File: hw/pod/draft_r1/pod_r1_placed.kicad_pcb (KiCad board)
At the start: 4 copper layers, 34 x 13 mm, 76 parts, among them J1 TestPoint_Pad_D1.0mm, J10 TestPoint_Pad_D1.0mm, J11 TestPoint_Pad_D1.0mm, J12 TestPoint_Pad_D1.0mm, J2 TestPoint_Pad_D1.0mm, J3 TestPoint_Pad_D1.0mm, J4 TestPoint_Pad_D1.0mm, J5 TestPoint_Pad_D1.0mm, J6 TestPoint_Pad_D1.0mm, J7 TestPoint_Pad_D1.0mm, J8 TestPoint_Pad_D1.0mm, J9 TestPoint_Pad_D1.0mm, Q1 SOT1216_L1.1-W1.0-P0.35-BL-EP, Q2 SOT1216_L1.1-W1.0-P0.35-BL-EP, SW1 SW-SMD_4P-L3.0-W2.6-P1.85-LS3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, U1 QFN-48-1EP_7x7mm_P0.5mm_EP5.6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, U2 Knowles_LGA-5_3.5x2.65mm, U3 DSBGA-8_L1.6-W0.9-R2-C4-P0.40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, U4 X2SON-4_L1.0-W1.0-P0.65-TL-EP, U6 SOT-553-5_L1.6-W1.2-P0.50-LS1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, Y1 FC-135R_L3.2-W1.5

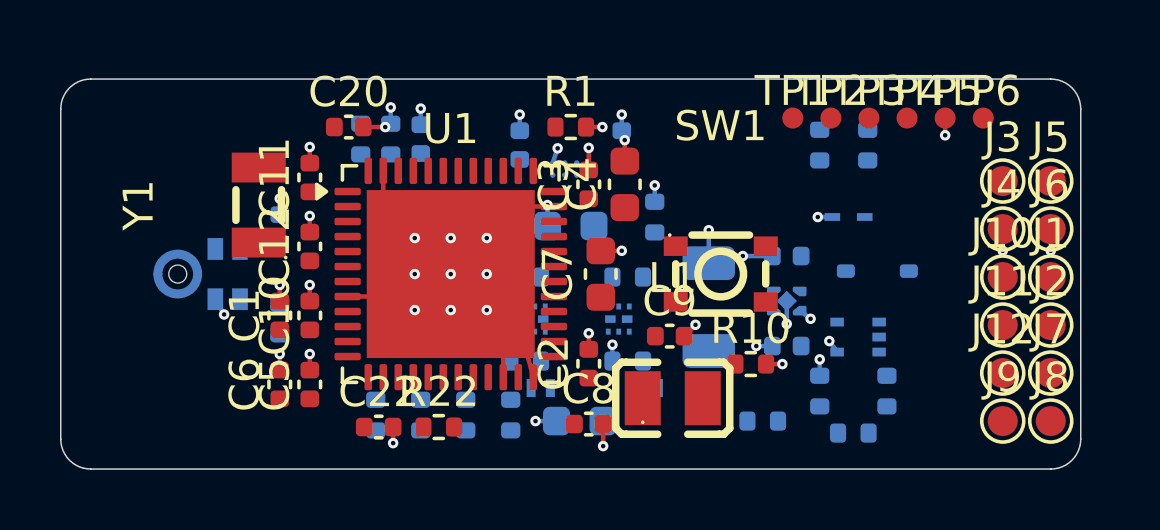
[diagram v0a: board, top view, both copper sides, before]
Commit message: Schematic Rev F (Phase 1 logical simplification, package B3): -R11 -R17 -R19 -C20 -D1/D2; PB5 GND strap (ECR-0013 S1); D3 -> D5 TPD1E10B06 at the J3 contact (Q31); J4+J6 -> one shared GND pad between DOCK_VBUS and VBAT (ASM-09); C15 25 V (ECR-0013 S3); TP7 printf + TP8-TP10 MDF fallback dots (PER-12); Q1/Q2 Nexperia land pattern (ECR-0004); kept R4/R6 (Q19), TP6, R22/C22, C14, R21 1206, CC + 5-contact dock, LED on the pad.
56 -> 52 placed parts, ERC 0. Placement re-done (0.8 mm board, C1 serves pins 1+48, rear pads re-ordered, charger cluster per ECR-0002). Contracts updated in the same commit; interfaces/bom_check/vcrm exit 0; self-tests updated for the new design.

Co-Authored-By: Claude Opus 5.5 <noreply@anthropic.com>
Claude-Session: https://claude.ai/code/session_01Wg997D6KFs8bxoAH56jZZJ
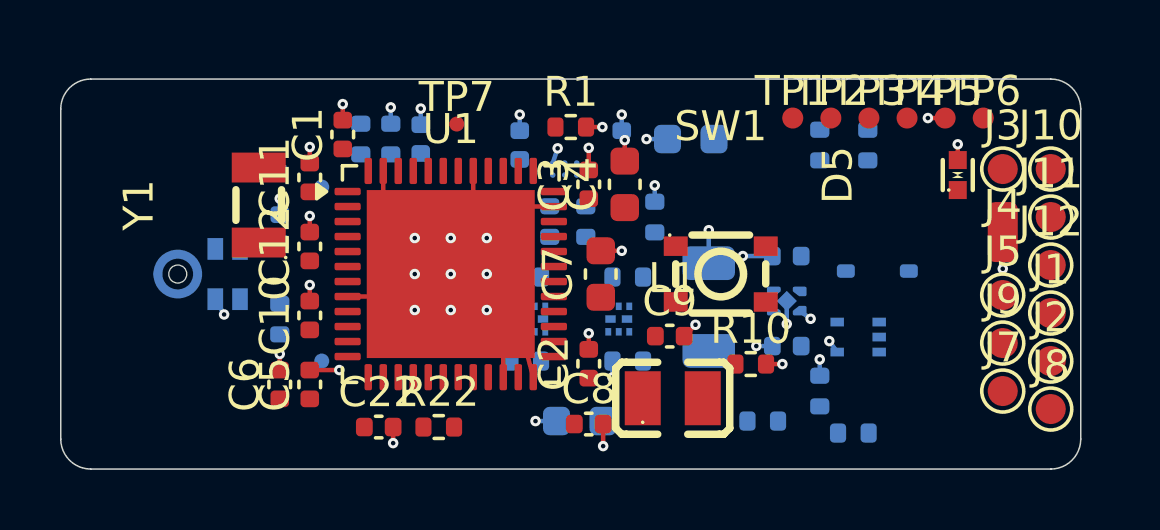
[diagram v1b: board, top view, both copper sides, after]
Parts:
- removed C20: C_0402_1005Metric, C_0402_1005Metric
- removed D1, D2: SOD-882_L1.0-W0.6-BI, SOD-882_L1.0-W0.6-BI
- removed D3: SOD-923_L0.8-W0.6-LS1.0-RD, SOD-923_L0.8-W0.6-LS1.0-RD
- removed J6: TestPoint_Pad_D1.0mm, TestPoint_Pad_D1.0mm
- removed R11, R17, R19: R_0402_1005Metric, R_0402_1005Metric
- added D5: X1SON-2_L1.0-W0.6-P0.65-BI-1, X1SON-2_L1.0-W0.6-P0.65-BI-1, F.Cu at (29.9, 3.20)
- added TP10: TestDot_D0.5mm, TestDot_D0.5mm, B.Cu at (7.30, 3.00)
- added TP7: TestDot_D0.5mm, TestDot_D0.5mm, F.Cu at (13.2, 1.50)
- added TP8: TestDot_D0.5mm, TestDot_D0.5mm, B.Cu at (8.70, 9.40)
- added TP9: TestDot_D0.5mm, TestDot_D0.5mm, B.Cu at (8.70, 3.60)
- J4: value TestPoint_Pad_D1.0mm -> WirePad_1.0x2.0mm; footprint TestPoint_Pad_D1.0mm -> WirePad_1.0x2.0mm
- Q1, Q2: value SOT1216_L1.1-W1.0-P0.35-BL-EP -> Nexperia_SOT1216_DFN1010B-6; footprint SOT1216_L1.1-W1.0-P0.35-BL-EP -> Nexperia_SOT1216_DFN1010B-6
- moved R15 8.48 mm to (17.5, 4.75), turned to -90 degrees
- moved R16 7.03 mm to (16.3, 4.75), turned to -90 degrees
- moved C1 6.39 mm to (9.40, 1.85)
- moved C21 4.94 mm to (21.0, 2.00)
- moved J5 4.12 mm to (31.4, 7.20)
- moved J10 3.94 mm to (33.0, 3.00)
- moved J12 3.94 mm to (33.0, 6.20)
- moved J11 3.94 mm to (33.0, 4.60)
- moved C15 3.40 mm to (18.7, 2.20)
- moved C16 3.40 mm to (15.3, 2.20)
- moved J9 2.60 mm to (31.4, 8.80)
- moved J7 1.71 mm to (31.4, 10.4)
- moved J2 1.20 mm to (33.0, 9.40)
- moved J1 1.20 mm to (33.0, 7.80)
- moved J8 0.40 mm to (33.0, 11.0)
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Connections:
- U1 pad 13: CC_SENSE -> (no net)
- U1 pad 19: (no net) -> MDF_SDI
- U1 pad 31: N$3 -> (no net)
- U1 pad 41: (no net) -> GND
- U1 pad 42: (no net) -> DBG_TX
- U1 pad 45: (no net) -> MDF_CCK
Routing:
- net GND: track 27.9 -> 28.3 mm, vias 47 -> 45
